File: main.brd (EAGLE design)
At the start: 146.5 x 85 mm, 61 parts, among them IC1 REG1117, X1 ZX62D-B-5PA8

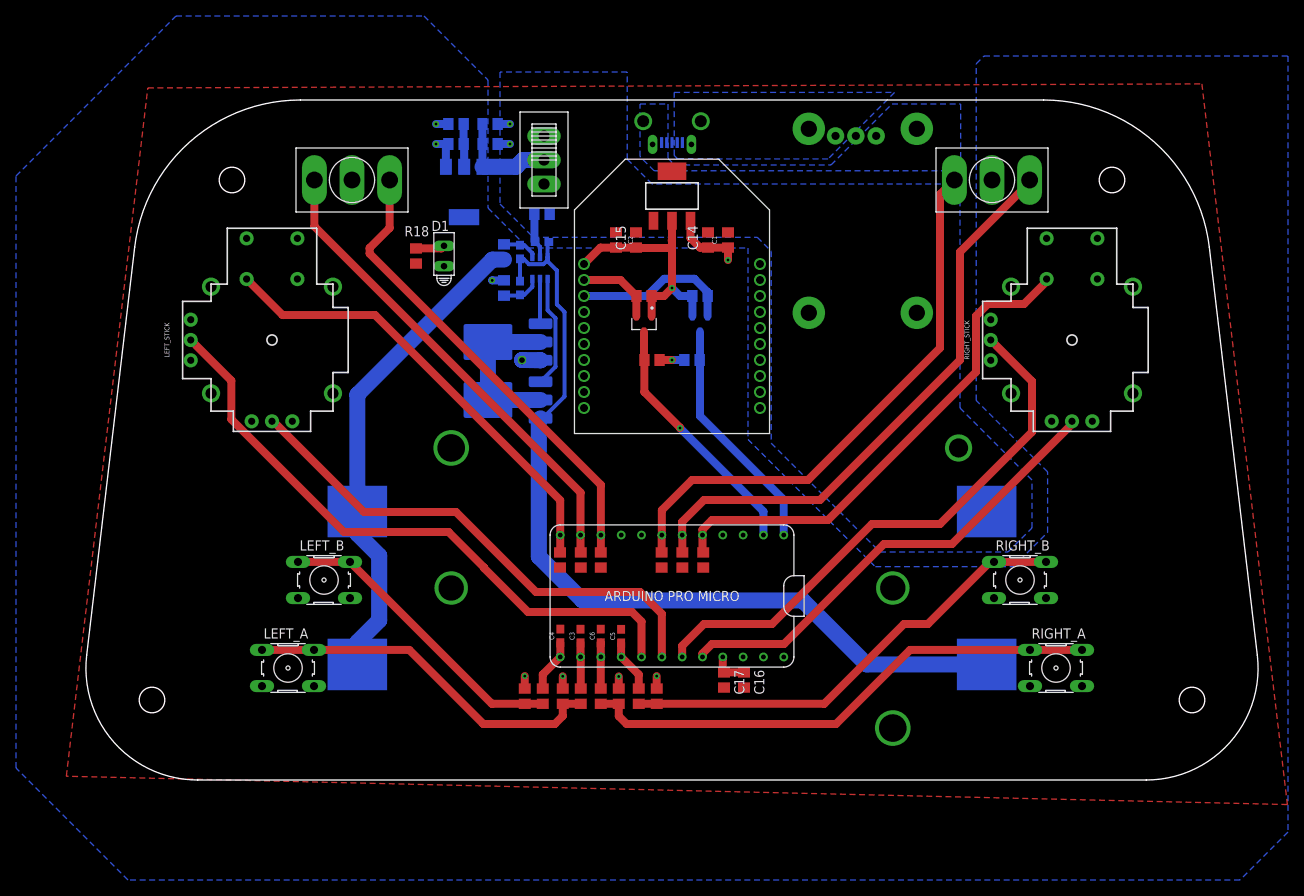
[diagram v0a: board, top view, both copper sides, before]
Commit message: Made AA mount
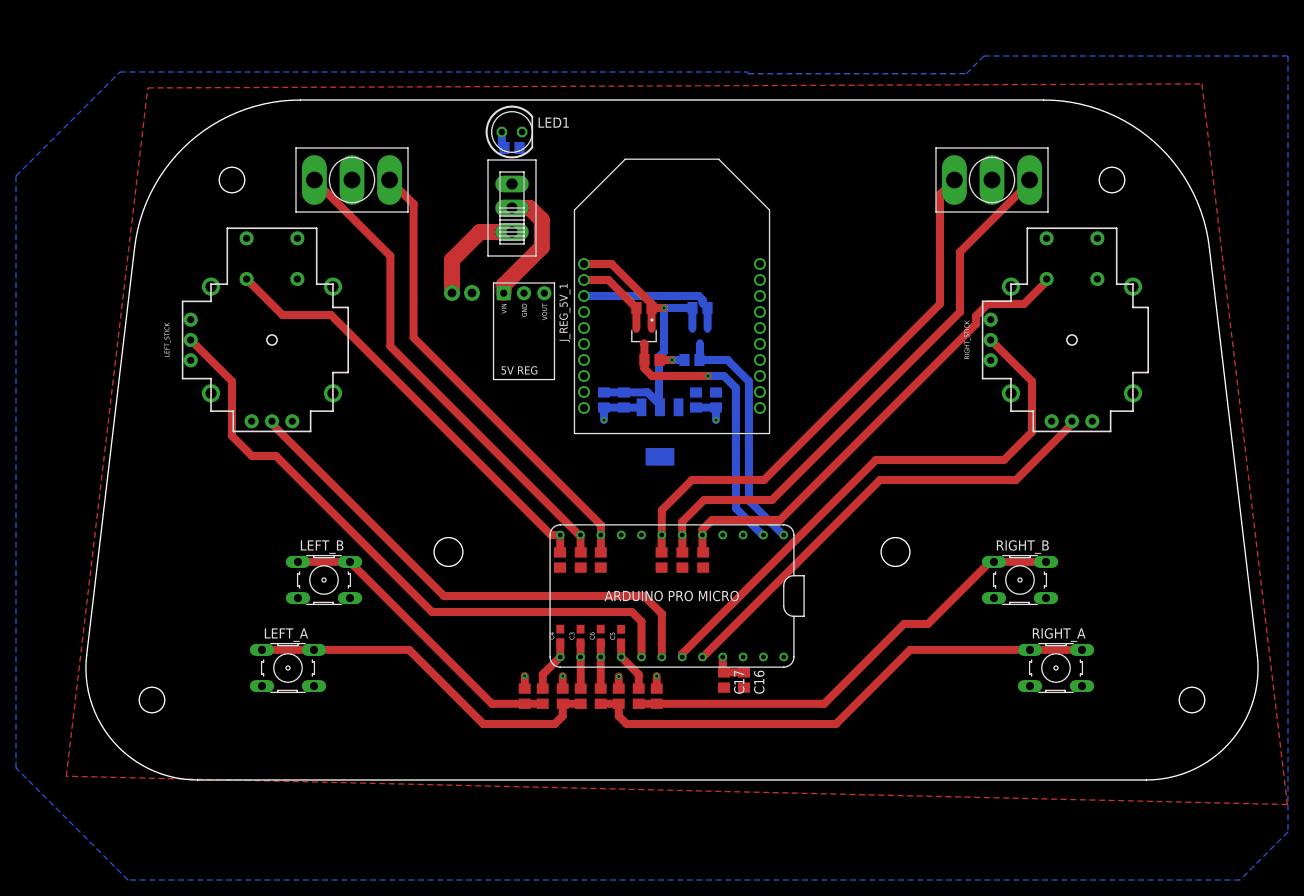
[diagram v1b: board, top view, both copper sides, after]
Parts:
- removed BT1: 1048, 1048:BAT_1048
- removed C10, C11: 0.1uF, rcl:C0805
- removed C12: 10uF, rcl:C0805
- removed C13: 22uF, rcl:C0805
- removed C7, C8: 0.1uF, SparkFun-Capacitors:0603
- removed C9: 0.01uF, SparkFun-Capacitors:0603
- removed D1: HLMP6, display-hp:HLMP6
- removed IC1: REG1117, burr-brown:SOT223
- removed NCH_C, NCH_D: FQD13N06LTM, Transistor:DPAK4
- removed R16: 1K, eagle-ltspice:R0805
- removed R17: 330R, eagle-ltspice:R0805
- removed R18: 470R, eagle-ltspice:R0805
- removed R5460: R5460, CustomParts:SOT-23-6
- removed U$6: EG1201, CustomParts:EG1201
- removed X1: ZX62D-B-5PA8, zx62d-b-5pa8-oshpark_10:ZX62D-B-5PA8
- added J_REG_5V_1: 5V_VOLTAGE_REGULATOR, Pololu Voltage Regulators:5V_VOLTAGE_REGULATOR
- added LED1: (no value), led:LED5MM
- added U$3: 4XAA, CustomParts:AA_HOLDER
- R15: value 330R -> 470R
- U$4: value TP5100_MODULE -> EG1201; device CustomParts:TP5100_MODULE -> CustomParts:EG1201
- moved U$4 43.5 mm to (-20.0, 28.0), flipped to the top, turned to 90 degrees
- moved 3V_SRC 29.5 mm to (-1.50, 0.00), flipped to the bottom, turned to 180 degrees
- moved C1 20.1 mm to (5.50, 4.00), flipped to the bottom, turned to 270 degrees
- moved C14 20.1 mm to (3.00, 4.00), flipped to the bottom, turned to 270 degrees
- moved C15 20.1 mm to (-6.00, 4.00), flipped to the bottom, turned to 270 degrees
- moved C2 20.1 mm to (-8.50, 4.00), flipped to the bottom, turned to 270 degrees
- moved R15 9.06 mm to (-20.0, 35.5)
- moved LLC_RX 1.50 mm to (3.50, 12.0)
- moved LLC_RX_LOW 1.50 mm to (3.50, 15.5)
- moved LLC_TX 1.50 mm to (-3.50, 12.0)
- moved LLC_TX_LOW 1.50 mm to (-3.50, 15.5)
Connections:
- removed net 8V4_IN: C10.1, C12.1, IC1.3, U$6.2
- removed net B+: BT1.C2+, R15.2, U$4.B+, U$6.1
- removed net BM: BT1.C1+, BT1.C2-, R17.1
- removed net COUT: NCH_C.1, R5460.2
- removed net DOUT: NCH_D.1, R5460.1
- removed net N$5: D1.K, R18.1
- removed net P+: U$4.P+, X1.1
- removed net P-: U$4.P-, X1.5
- removed net V-: C9.1, R16.2, R5460.3
- removed net VC: C8.1, R17.2, R5460.4
- removed net VDD: C7.1, R15.1, R5460.5
- removed net VSS: BT1.C1-, C7.2, C8.2, C9.2, NCH_D.3, R5460.6
- new net N$1: U$3.B+, U$4.1
- new net N$2: J_REG_5V_1.VIN, U$4.2
- net GND: now also J_REG_5V_1.GND, LED1.K, U$3.B-; no longer C10.2, C11.2, C12.2, C13.2, IC1.1, NCH_C.3, R16.1, R18.2, U$4.B-
- net N$3: now also LED1.A, R15.1; no longer NCH_C.2, NCH_C.4, NCH_D.2, NCH_D.4
- net VCC: now also J_REG_5V_1.VOUT, R15.2; no longer C11.1, C13.1, D1.A, IC1.2
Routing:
- net VSS: track 110.5 -> 0.00 mm
- net BM: track 61.4 -> 0.00 mm
- net N$3: track 20.4 -> 2.13 mm
- net N$2: track 0.00 -> 15.5 mm
- net VCC: track 28.1 -> 13.8 mm, vias 6 -> 5
- net DOUT: track 14.0 -> 0.00 mm
- net 8V4_IN: track 13.4 -> 0.00 mm
- net N$1: track 0.00 -> 13.1 mm
- net 3V3: track 31.3 -> 41.3 mm
- net VDD: track 5.69 -> 0.00 mm
- net COUT: track 5.64 -> 0.00 mm
- net V-: track 5.01 -> 0.00 mm
- net VC: track 4.51 -> 0.00 mm
- net TX: track 31.6 -> 35.5 mm
- net N$5: track 3.63 -> 0.00 mm
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- removed copper zone on layer 16, net B+
- removed copper zone on layer 16, net P+
- removed copper zone on layer 16, net P-

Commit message: Minor positioning changes
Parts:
- moved LED1 7.91 mm to (-26.5, 33.0)
- moved R15 7.83 mm to (-13.0, 32.0)
- moved U$4 1.00 mm to (-20.0, 27.0)
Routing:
- net N$3: track 2.13 -> 0.00 mm
- net N$2: track 15.5 -> 16.2 mm
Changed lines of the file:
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@@
 </element>
 <element name="U$3" library="CustomParts" package="AA_HOLDER" value="4XAA" x="0" y="-15" smashed="yes" rot="MR0"/>
-<element name="U$4" library="CustomParts" package="EG1201" value="EG1201" x="-20" y="28" smashed="yes" rot="R90"/>
-<element name="LED1" library="led" library_urn="urn:adsk.eagle:library:259" package="LED5MM" package3d_urn="urn:adsk.eagle:package:15799/2" value="" x="-20" y="37.5" smashed="yes">
-<attribute name="NAME" x="-16.825" y="38.0334" size="1.27" layer="25" ratio="10"/>
-<attribute name="VALUE" x="-16.7996" y="35.6966" size="1.27" layer="27" ratio="10"/>
+<element name="U$4" library="CustomParts" package="EG1201" value="EG1201" x="-20" y="27" smashed="yes" rot="R90"/>
+<element name="LED1" library="led" library_urn="urn:adsk.eagle:library:259" package="LED5MM" package3d_urn="urn:adsk.eagle:package:15799/2" value="" x="-26.5" y="33" smashed="yes">
+<attribute name="NAME" x="-23.325" y="33.5334" size="1.27" layer="25" ratio="10"/>
+<attribute name="VALUE" x="-23.2996" y="31.1966" size="1.27" layer="27" ratio="10"/>
 </element>
-<element name="R15" library="eagle-ltspice" library_urn="urn:adsk.eagle:library:217" package="R0805" package3d_urn="urn:adsk.eagle:package:13300/1" value="470R" x="-20" y="35.5" smashed="yes" rot="MR180">
-<attribute name="NAME" x="-20.635" y="34.23" size="1.27" layer="26" rot="MR180"/>
-<attribute name="SPICEMODEL" value="NONE" x="-20" y="35.5" size="1.778" layer="28" rot="MR180" display="off"/>
-<attribute name="SPICEPREFIX" value="R" x="-20" y="35.5" size="1.778" layer="28" rot="MR180" display="off"/>
-<attribute name="VALUE" x="-20.635" y="38.04" size="1.27" layer="28" rot="MR180"/>
+<element name="R15" library="eagle-ltspice" library_urn="urn:adsk.eagle:library:217" package="R0805" package3d_urn="urn:adsk.eagle:package:13300/1" value="470R" x="-13" y="32" smashed="yes" rot="MR180">
+<attribute name="NAME" x="-13.635" y="30.73" size="1.27" layer="26" rot="MR180"/>
+<attribute name="SPICEMODEL" value="NONE" x="-13" y="32" size="1.778" layer="28" rot="MR180" display="off"/>
+<attribute name="SPICEPREFIX" value="R" x="-13" y="32" size="1.778" layer="28" rot="MR180" display="off"/>
+<attribute name="VALUE" x="-13.635" y="34.54" size="1.27" layer="28" rot="MR180"/>
 </element>
 </elements>
@@
 <contactref element="J_REG_5V_1" pad="VOUT"/>
 <contactref element="R15" pad="2"/>
+<wire x1="-15.96" y1="17.35" x2="-12.05" y2="32" width="0" layer="19" extent="1-1"/>
 </signal>
 <signal name="N$2">
 <contactref element="U$4" pad="2"/>
 <contactref element="J_REG_5V_1" pad="VIN"/>
-<wire x1="-16.273" y1="26.5" x2="-17.773" y2="28" width="2" layer="1"/>
-<wire x1="-20" y1="28" x2="-17.773" y2="28" width="2" layer="1"/>
-<wire x1="-16.273" y1="26.5" x2="-16.273" y2="23.117" width="2" layer="1"/>
-<wire x1="-16.273" y1="23.117" x2="-21.04" y2="18.35" width="2" layer="1"/>
-<wire x1="-21.04" y1="17.35" x2="-21.04" y2="18.35" width="2" layer="1"/>
+<wire x1="-20" y1="27" x2="-16.273" y2="27" width="2" layer="1"/>
+<wire x1="-16.273" y1="27" x2="-16.273" y2="20.617" width="2" layer="1"/>
+<wire x1="-16.273" y1="20.617" x2="-19.54" y2="17.35" width="2" layer="1"/>
+<wire x1="-21.04" y1="17.35" x2="-19.54" y2="17.35" width="2" layer="1"/>
 </signal>
 <signal name="N$3">
 <contactref element="LED1" pad="A"/>
 <contactref element="R15" pad="1"/>
-<wire x1="-20.95" y1="35.5" x2="-21.27" y2="35.82" width="1" layer="16"/>
-<wire x1="-21.27" y1="35.82" x2="-21.27" y2="37.5" width="1" layer="16"/>
+<wire x1="-27.77" y1="33" x2="-13.95" y2="32" width="0" layer="19" extent="1-1"/>
 </signal>
 <signal name="N$1">
@@
 <contactref element="U$3" pad="B+"/>
 <wire x1="-27.5" y1="17.38" x2="-27.5" y2="21.5" width="2" layer="1"/>
-<wire x1="-24" y1="25" x2="-20" y2="25" width="2" layer="1"/>
-<wire x1="-24" y1="25" x2="-27.5" y2="21.5" width="2" layer="1"/>
+<wire x1="-25" y1="24" x2="-20" y2="24" width="2" layer="1"/>
+<wire x1="-25" y1="24" x2="-27.5" y2="21.5" width="2" layer="1"/>
 </signal>
 </signals>

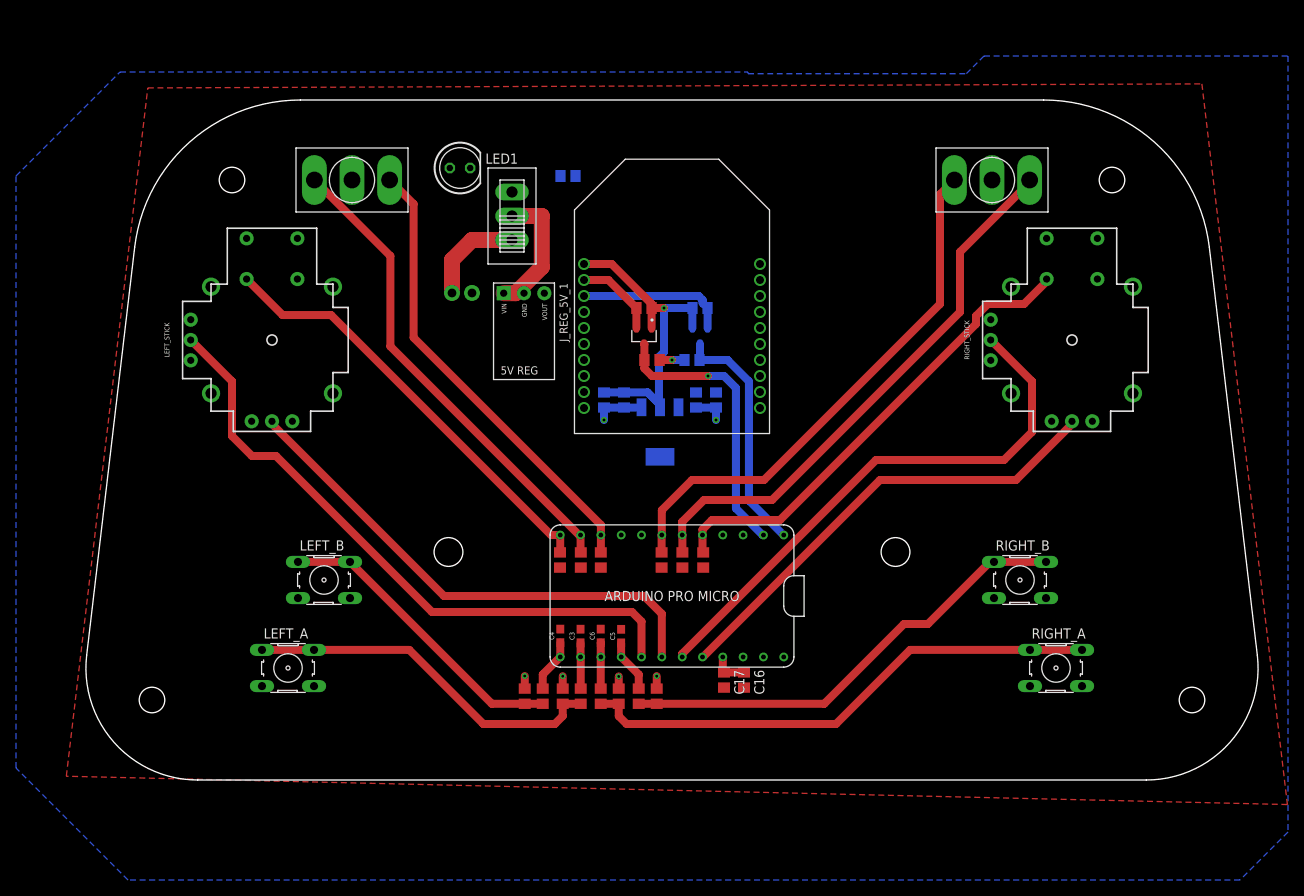
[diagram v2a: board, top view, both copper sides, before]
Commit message: Made silkscreen touches
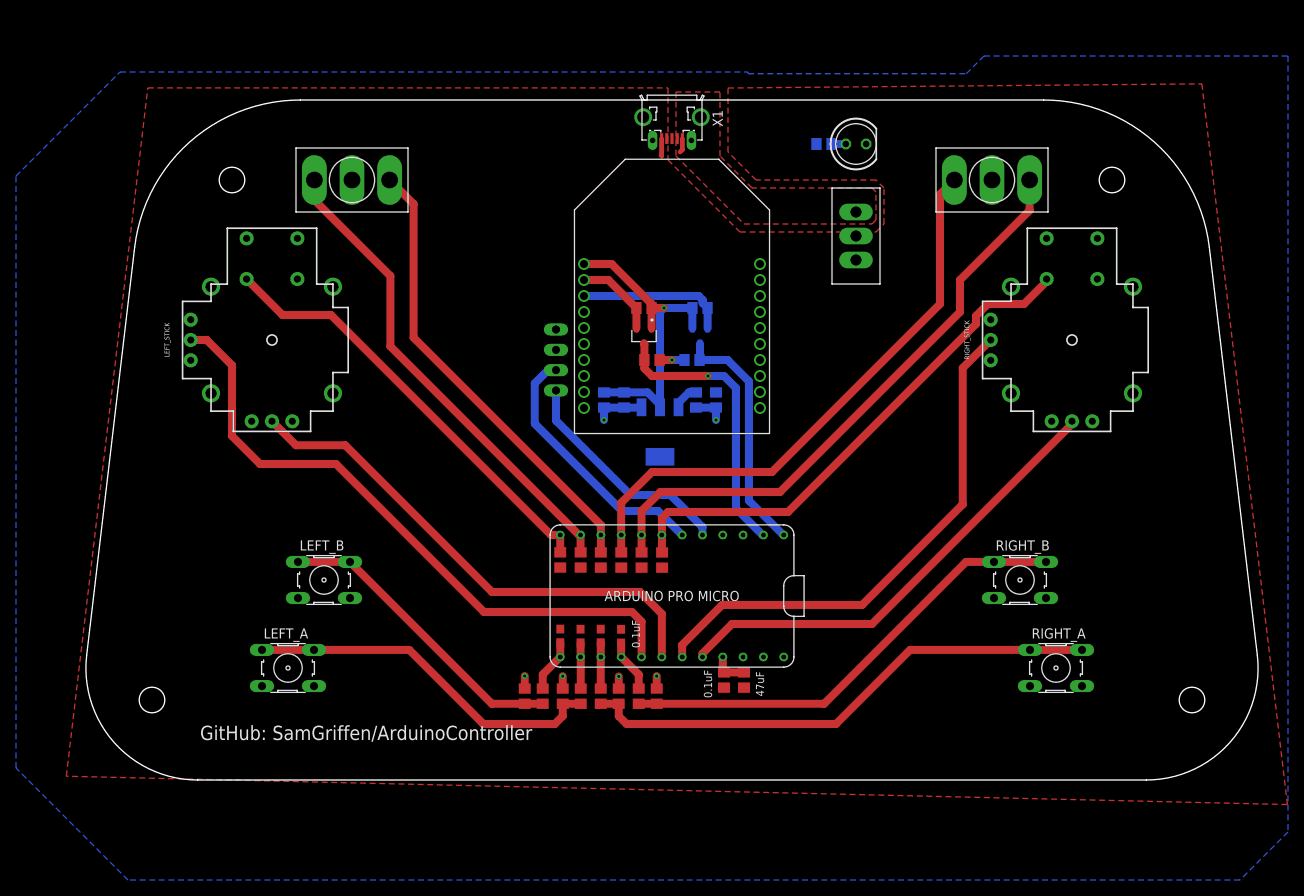
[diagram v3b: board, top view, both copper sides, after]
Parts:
- removed J_REG_5V_1: 5V_VOLTAGE_REGULATOR, Pololu Voltage Regulators:5V_VOLTAGE_REGULATOR
- removed U$3: 4XAA, CustomParts:AA_HOLDER
- added SV3: (no value), con-lstb:MA04-1
- added X1: ZX62D-B-5PA8, zx62d-b-5pa8-oshpark_10:ZX62D-B-5PA8
- R15: value 470R -> 470
- moved LED1 49.6 mm to (23.0, 36.0)
- moved U$4 43.1 mm to (23.0, 24.5)
- moved R15 32.2 mm to (19.0, 36.0), turned to 0 degrees
- moved R14 5.14 mm to (-1.24, -16.0)
- moved R9 5.10 mm to (-3.80, -16.0)
- moved R10 5.04 mm to (-6.34, -16.0)
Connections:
- removed net N$1: U$3.B+, U$4.1
- removed net N$2 (its old number): J_REG_5V_1.VIN, U$4.2
- new net INPUT_V: U$4.3, X1.1
- new net SCL: SV3.2, U$1.3
- new net SDA: SV3.1, U$1.2
- net GND: now also SV3.3, X1.5; no longer J_REG_5V_1.GND, U$3.B-
- net RIGHT_STICK_SW: now also U$1.4; no longer U$1.2
- net RIGHT_SW_A: now also U$1.5; no longer U$1.3
- net RIGHT_SW_B: now also U$1.6; no longer U$1.4
- net VCC: now also SV3.4, U$4.2; no longer J_REG_5V_1.VOUT
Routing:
- net SCL: track 0.00 -> 32.6 mm
- net SDA: track 0.00 -> 28.6 mm
- net N$2 (its old number): track 16.2 -> 0.00 mm
- net N$1: track 12.7 -> 0.00 mm
- net RIGHT_STICK_SW: track 59.6 -> 65.5 mm
- net RIGHT_SW_A: track 69.5 -> 75.4 mm
- net RIGHT_SW_B: track 67.0 -> 72.6 mm
- net RIGHT_Y: track 69.2 -> 65.8 mm
- net VCC: track 13.8 -> 17.1 mm
- net GND: track 10.3 -> 12.5 mm
- net INPUT_V: track 0.00 -> 1.80 mm
- net N$2: track 0.00 -> 1.78 mm
- net LEFT_Y: track 79.4 -> 80.5 mm
- added copper zone on layer 1, net INPUT_V
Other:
- board text added: "0.1uF"
- board text added: "100nF"
- board text added: "10uF"
- board text added: "22uF"
- board text added: "470R"
- board text added: "47uF"
- board text added: "GND"
- board text added: "GitHub: SamGriffen/ArduinoController"
- board text added: "I2C HEADER"
- board text added: "SCL"
- board text added: "SDA"
- board text added: "VCC"
